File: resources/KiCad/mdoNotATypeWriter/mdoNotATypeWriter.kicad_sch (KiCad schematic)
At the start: 4 parts

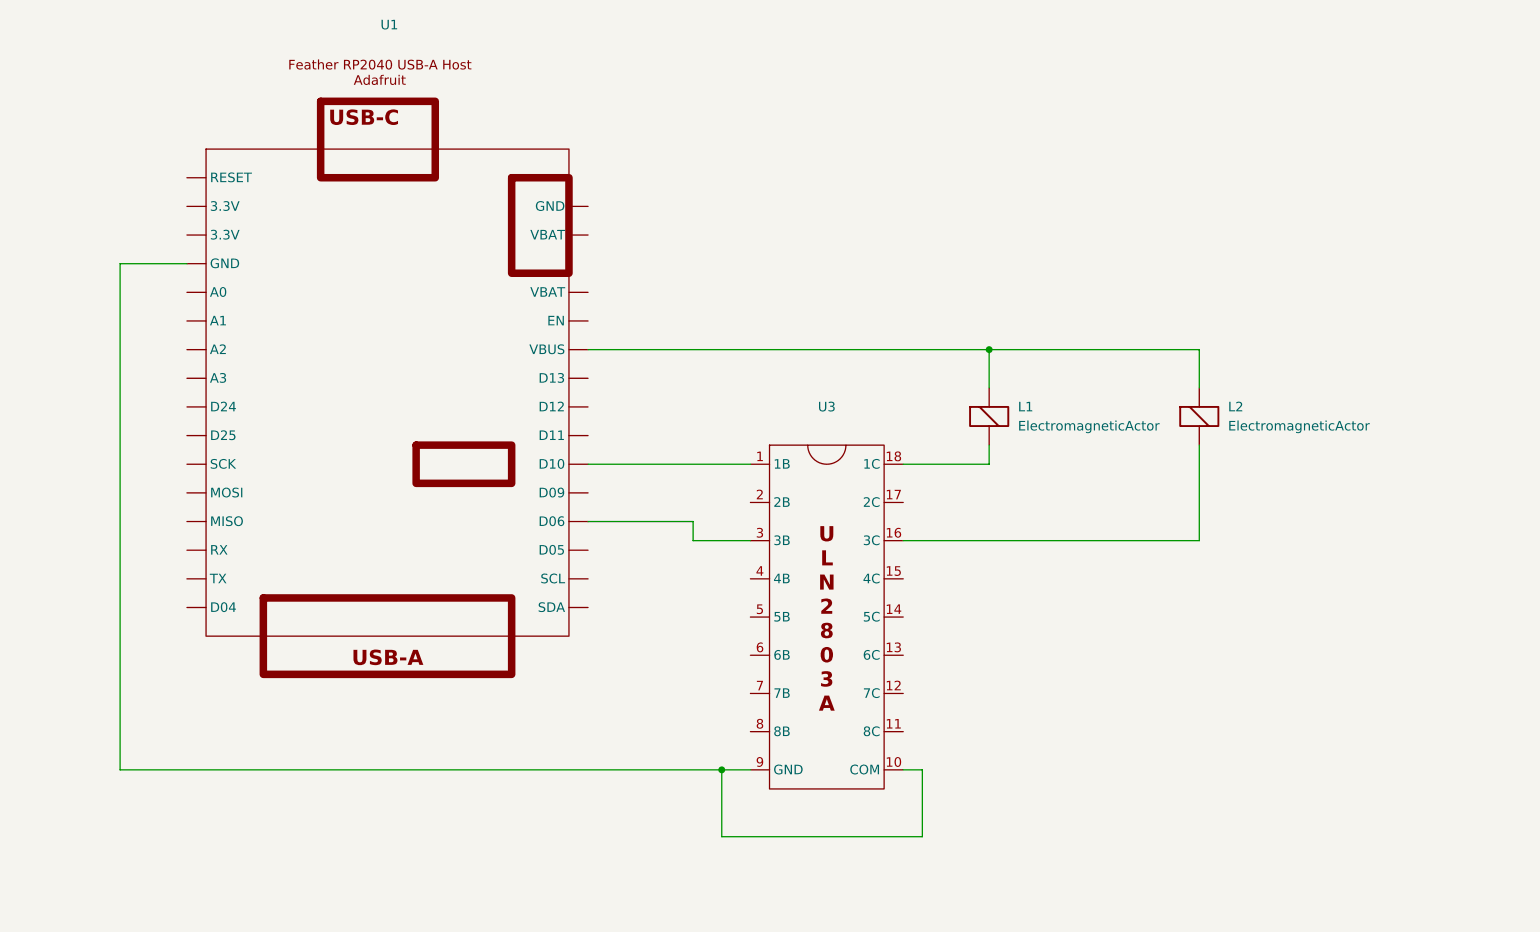
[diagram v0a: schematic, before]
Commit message: update schematic
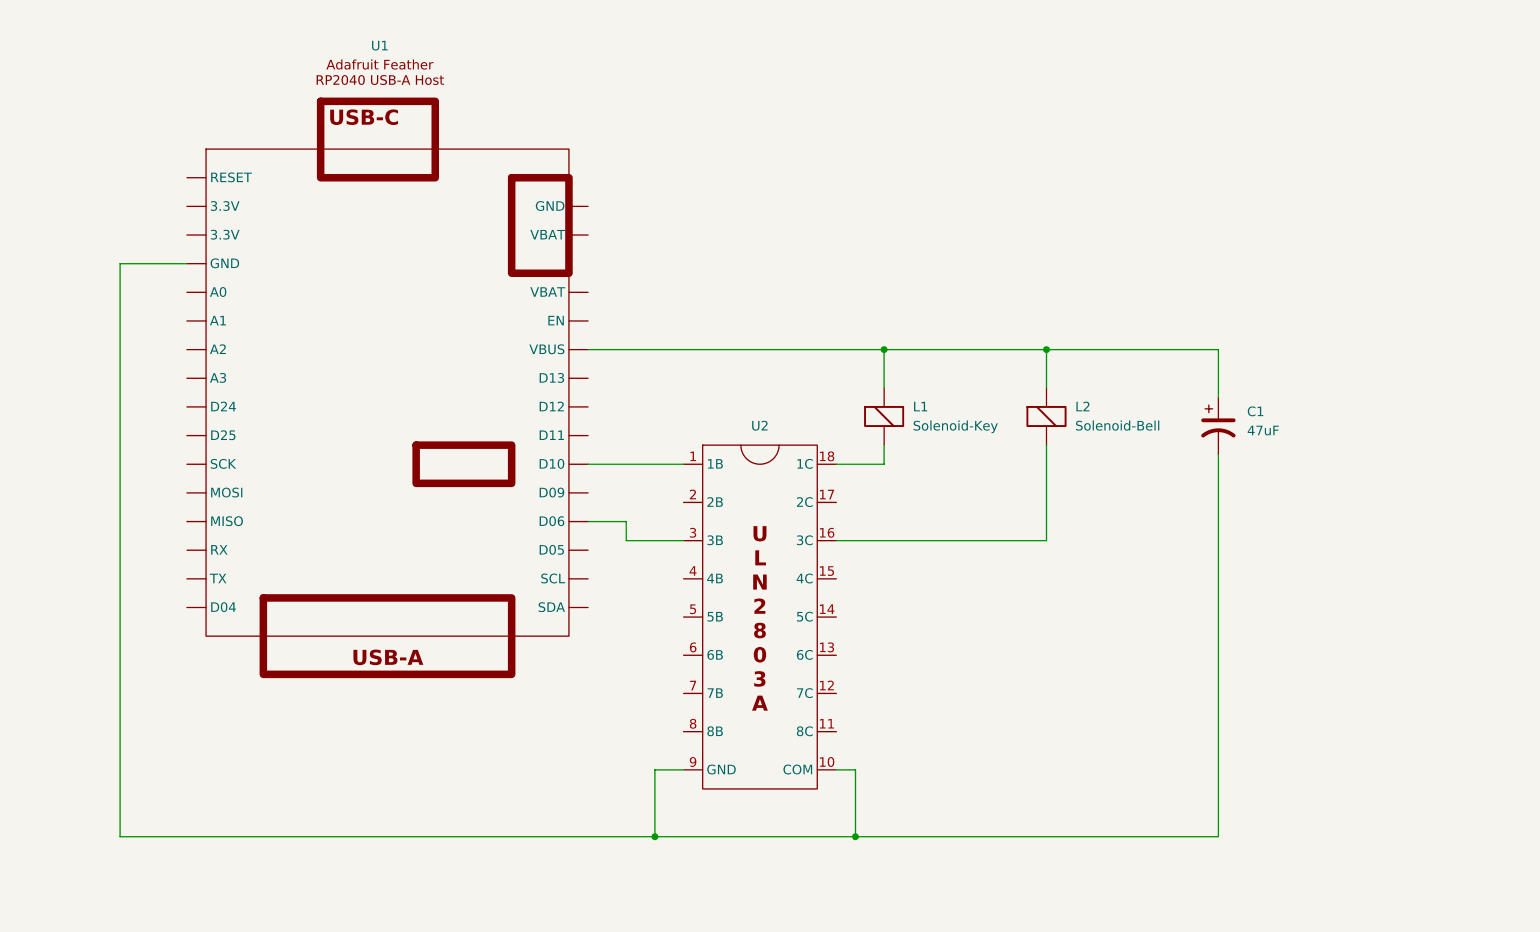
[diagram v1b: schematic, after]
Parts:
- added C1: 47uF, symbol Device:C_Polarized_US
- L1: value ElectromagneticActor -> Solenoid-Key
- L2: value ElectromagneticActor -> Solenoid-Bell
- renumbered U3 to U2
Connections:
- net at U1. (SDA), U2.10 (COM), U2.9 (GND): now also C1.2
- net at L1.1 (-), L2.1 (-), U1. (SDA): now also C1.1
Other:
- moved on the sheet: L1, L2, U2

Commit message: fix connection to ULN2803A COM
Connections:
- net at C1.2, U1. (SDA), U2.9 (GND): no longer U2.10 (COM)
- net at C1.1, L1.1 (-), L2.1 (-)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: now also U2.10 (COM)
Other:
- moved on the sheet: C1
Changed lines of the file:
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@@
 	(title_block
 		(title "mdoNotATypeWriter")
-		(date "2025-08-01")
-		(rev "Rev 0.9.1")
+		(date "2025-08-06")
+		(rev "Rev 0.9.2")
 		(company "https://github.com/Mark-MDO47")
+	)
+	(junction
+		(at 208.28 76.2)
+		(diameter 0)
+		(color 0 0 0 0)
 	)
 	(junction
@@
 	)
 	(junction
-		(at 162.56 140.97)
-		(diameter 0)
-		(color 0 0 0 0)
-	)
-	(junction
 		(at 135.89 140.97)
 		(diameter 0)
@@
 	(wire
 		(pts
-			(xy 162.56 132.08) (xy 162.56 140.97)
-		)
-		(stroke
-			(width 0)
-			(type default)
-		)
-	)
-	(wire
-		(pts
 			(xy 166.37 76.2) (xy 187.96 76.2)
 		)
@@
 	(wire
 		(pts
-			(xy 210.82 82.55) (xy 210.82 76.2)
+			(xy 208.28 76.2) (xy 217.17 76.2)
+		)
+		(stroke
+			(width 0)
+			(type default)
+		)
+	)
+	(wire
+		(pts
+			(xy 217.17 82.55) (xy 217.17 76.2)
 		)
 		(stroke
@@
 	(wire
 		(pts
-			(xy 210.82 90.17) (xy 210.82 140.97)
+			(xy 217.17 90.17) (xy 217.17 140.97)
 		)
 		(stroke
@@
 	(wire
 		(pts
-			(xy 210.82 140.97) (xy 162.56 140.97)
-		)
-		(stroke
-			(width 0)
-			(type default)
-		)
-	)
-	(wire
-		(pts
 			(xy 135.89 140.97) (xy 64.77 140.97)
 		)
@@
 	(wire
 		(pts
-			(xy 210.82 76.2) (xy 187.96 76.2)
+			(xy 187.96 76.2) (xy 208.28 76.2)
+		)
+		(stroke
+			(width 0)
+			(type default)
+		)
+	)
+	(wire
+		(pts
+			(xy 135.89 140.97) (xy 217.17 140.97)
 		)
 		(stroke
@@
 	(wire
 		(pts
-			(xy 160.02 132.08) (xy 162.56 132.08)
+			(xy 160.02 132.08) (xy 208.28 132.08)
+		)
+		(stroke
+			(width 0)
+			(type default)
+		)
+	)
+	(wire
+		(pts
+			(xy 208.28 76.2) (xy 208.28 132.08)
 		)
 		(stroke
@@
 		(pts
 			(xy 187.96 88.9) (xy 187.96 101.6)
-		)
-		(stroke
-			(width 0)
-			(type default)
-		)
-	)
-	(wire
-		(pts
-			(xy 162.56 140.97) (xy 135.89 140.97)
 		)
 		(stroke
@@
 	(symbol
 		(lib_id "Device:C_Polarized_US")
-		(at 210.82 86.36 0)
+		(at 217.17 86.36 0)
 		(unit 1)
 		(exclude_from_sim no)
@@
 		(fields_autoplaced yes)
 		(property "Reference" "C1"
-			(at 214.63 84.4549 0)
+			(at 220.98 84.4549 0)
 			(effects
 				(font
@@
 		)
 		(property "Value" "47uF"
-			(at 214.63 86.9949 0)
+			(at 220.98 86.9949 0)
 			(effects
 				(font
@@
 		)
 		(property "Footprint" ""
-			(at 210.82 86.36 0)
+			(at 217.17 86.36 0)
 			(effects
 				(font
@@
 		)
 		(property "Datasheet" "~"
-			(at 210.82 86.36 0)
+			(at 217.17 86.36 0)
 			(effects
 				(font
@@
 		)
 		(property "Description" "Polarized capacitor, US symbol"
-			(at 210.82 86.36 0)
-			(effects
-				(font
+			(at 217.17 86.36 0)
+			(effects
+				(font

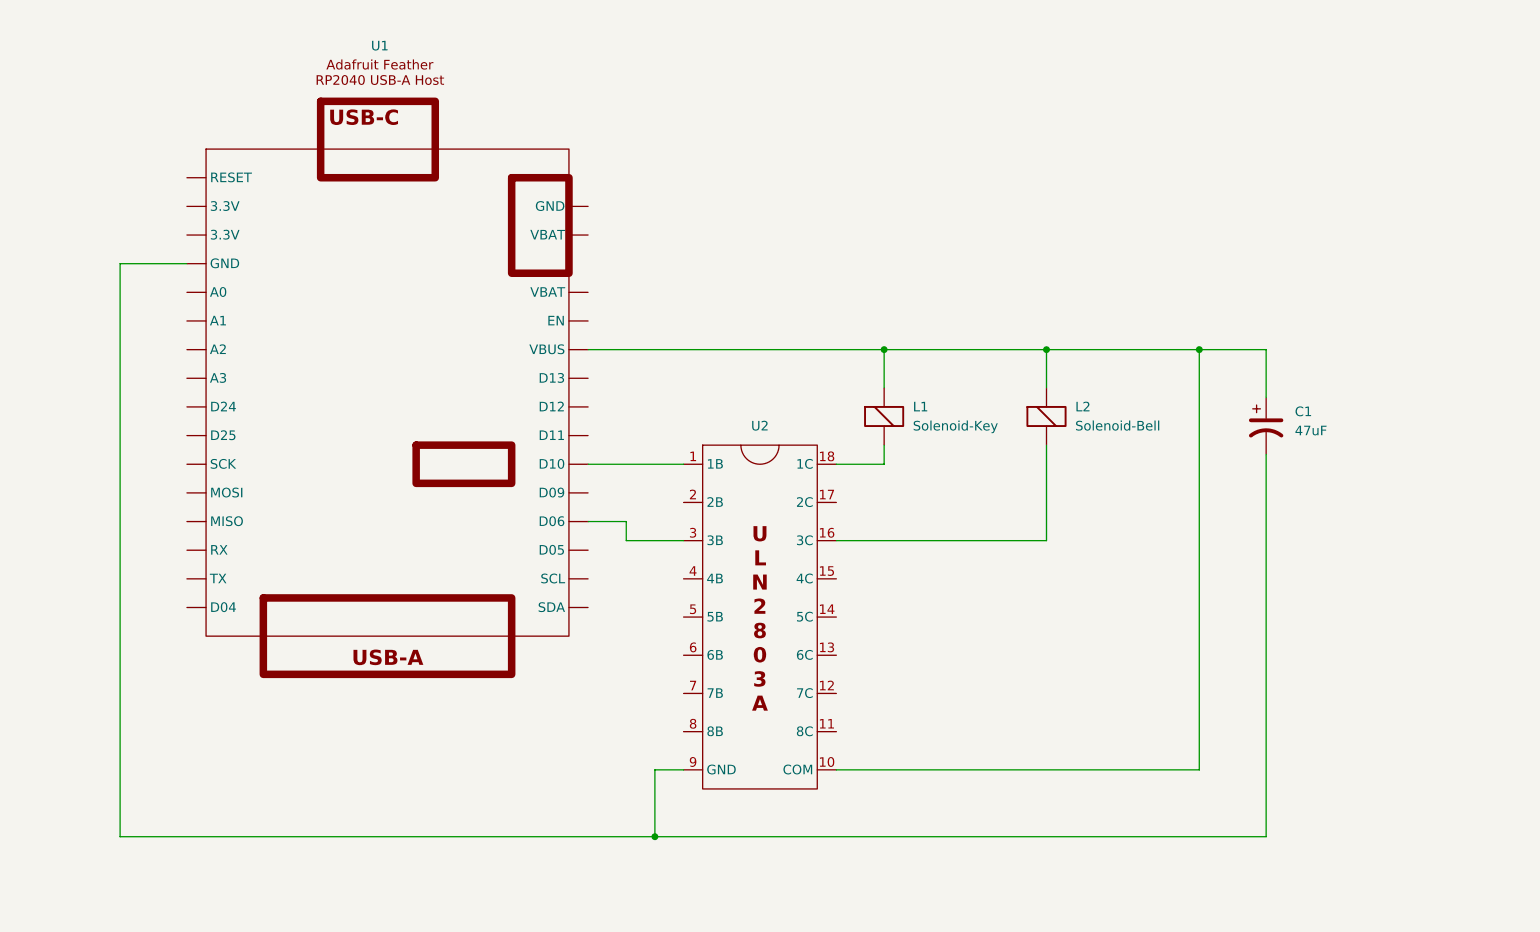
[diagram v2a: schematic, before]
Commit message: add LEDs and switch
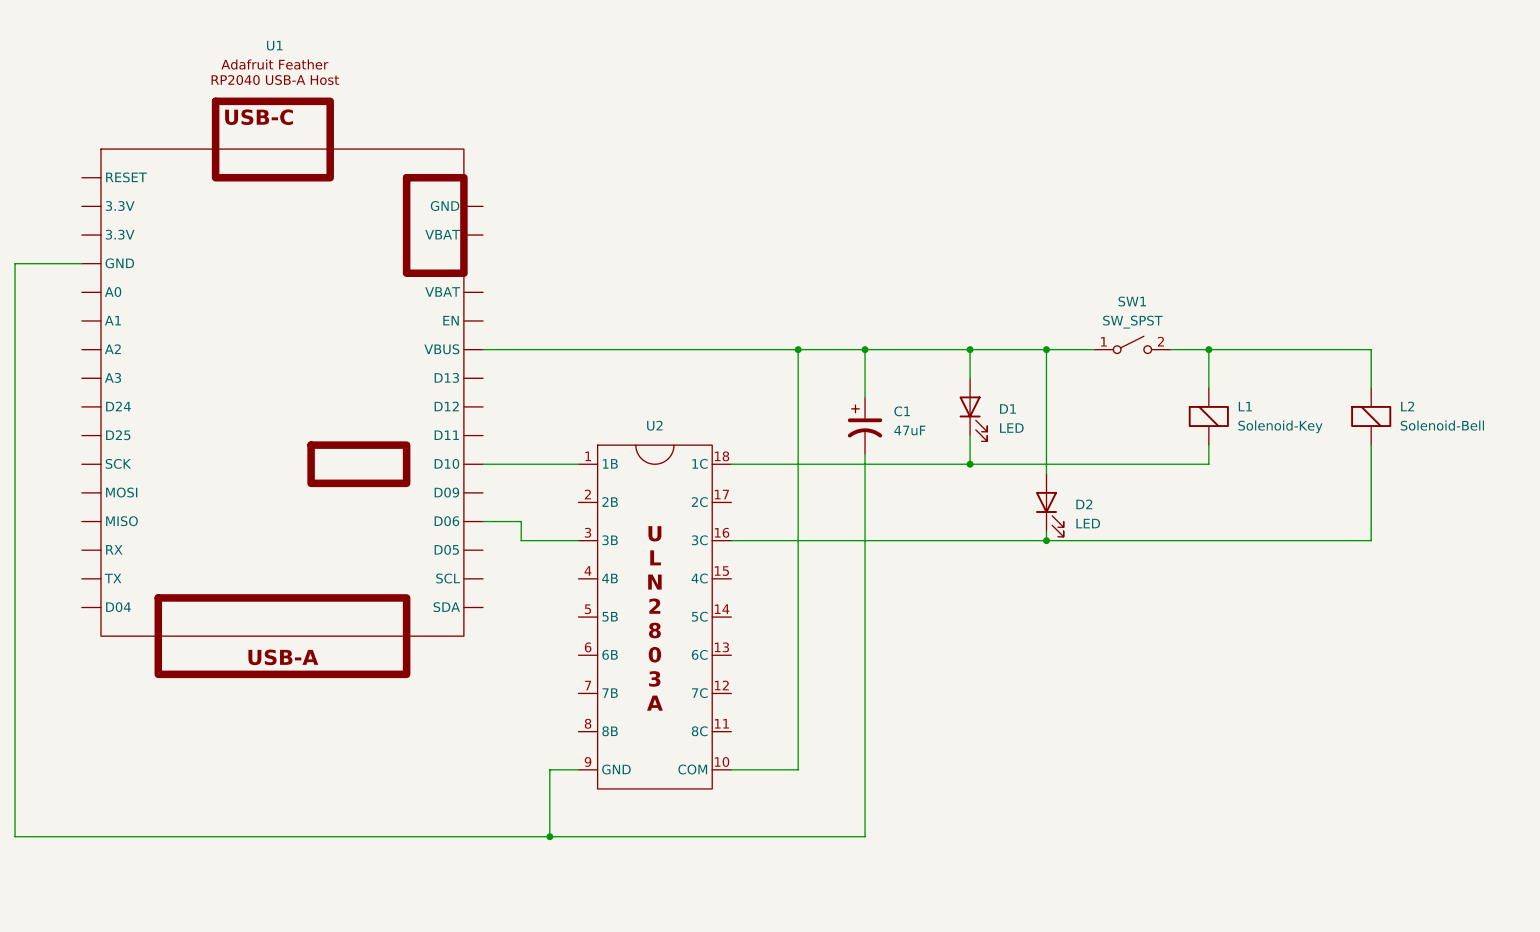
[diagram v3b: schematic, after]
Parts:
- added D1, D2: LED, symbol Device:LED
- added SW1: SW_SPST, symbol Switch:SW_SPST
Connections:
- net at L2.2 (+), U2.16 (3C): now also D2.1 (K)
- net at L1.2 (+), U2.18 (1C): now also D1.1 (K)
- new net: C1.1, D1.2 (A), D2.2 (A), SW1.1 (A), U1. (SDA), U2.10 (COM)
- new net: L1.1 (-), L2.1 (-), SW1.2 (B)
- now unconnected: U1. (SDA)
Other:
- company: https://github.com/Mark-MDO47 -> https://github.com/Mark-MDO47/mdoNotATypeWriter
- moved on the sheet: C1, L1, L2, U1, U2

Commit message: add resistors for LEDs
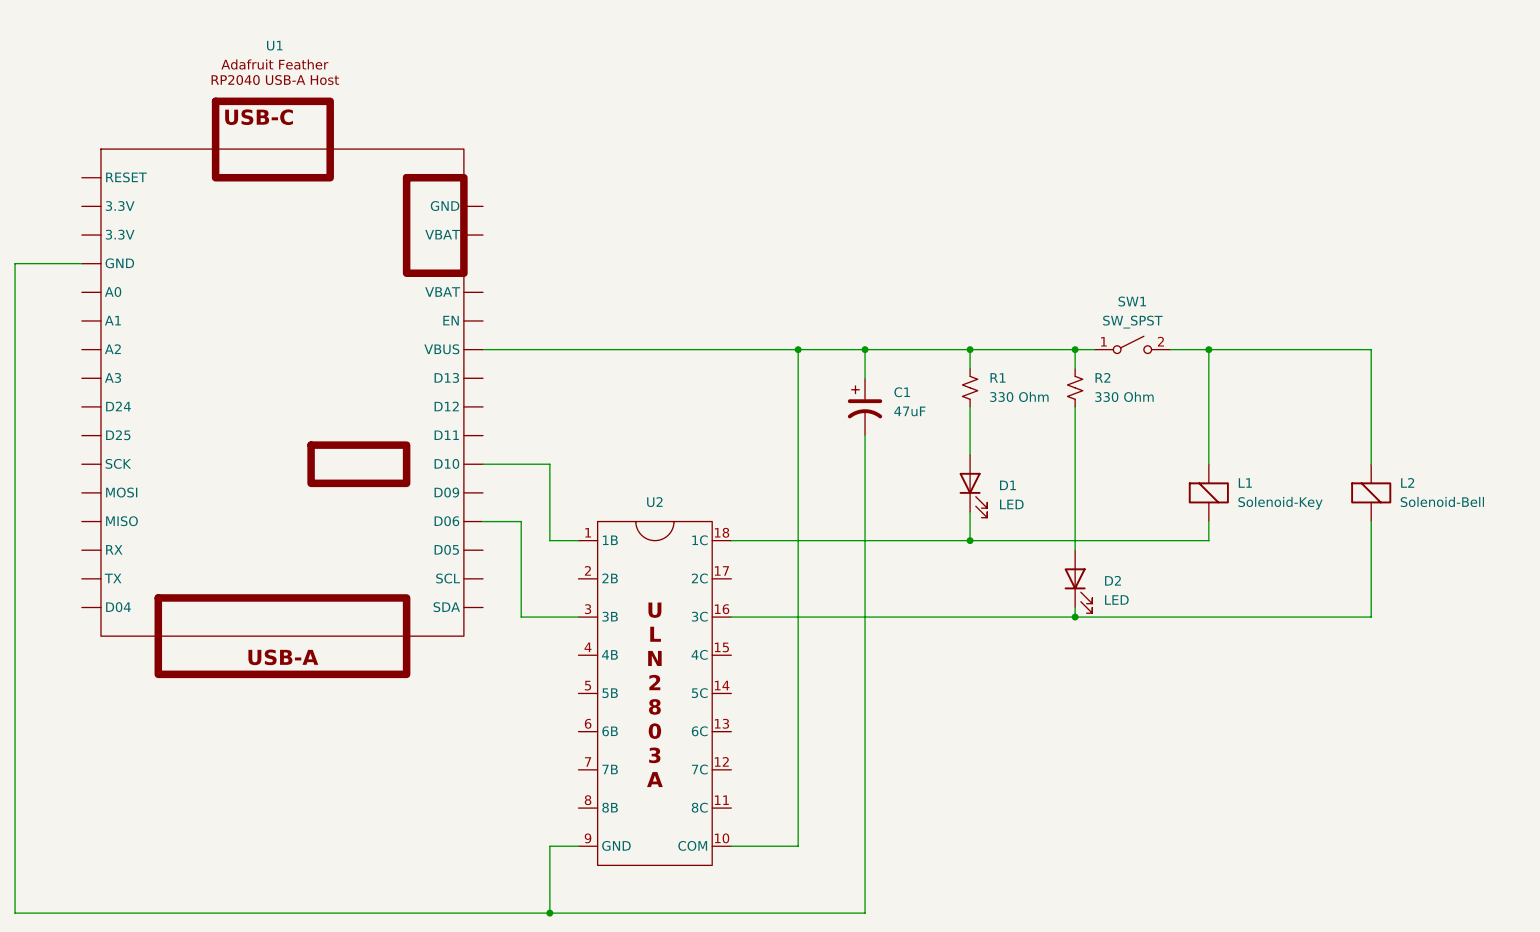
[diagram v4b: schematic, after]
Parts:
- added R1, R2: 330 Ohm, symbol Device:R_Small_US
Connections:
- net at C1.1, SW1.1 (A), U1. (SDA)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: now also R1.1, R2.1; no longer D1.2 (A), D2.2 (A)
- new net: D1.2 (A), R1.2
- new net: D2.2 (A), R2.2
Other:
- moved on the sheet: C1, D1, D2, L1, L2, U2

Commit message: Use StripPerfBoard, 100 uF cap
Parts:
- C1: value 47uF -> 100uF
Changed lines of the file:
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@@
 			)
 		)
-		(property "Value" "47uF"
+		(property "Value" "100uF"
 			(at 167.64 84.4549 0)
 			(effects
